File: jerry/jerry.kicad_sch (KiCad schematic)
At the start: 7 parts, among them U1 RASPBERRY_PI_4B_4GB

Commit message: Imported Parts
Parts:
- added J1, J2, J3: 0532610471, symbol jerry:0532610471
- added J4: XT60-M, symbol jerry:XT60-M
- added J7, J8: TSW-106-06-F-S-LL, symbol jerry:TSW-106-06-F-S-LL
- added U2: A4988_STEPPER_MOTOR_DRIVER_CARRIER, symbol jerry:A4988_STEPPER_MOTOR_DRIVER_CARRIER
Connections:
- new net: U2.15 (GND), U2.9 (GND)
- new net: J3.S1 (SHIELD), J3.S2 (SHIELD)
- new net: J1.S1 (SHIELD), J1.S2 (SHIELD)
- new net: J2.S1 (SHIELD), J2.S2 (SHIELD)
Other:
- moved on the sheet: D1, D2, D3, D4, D5, D6

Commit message: some updates
updated schematic, added components
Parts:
- added C1, C2, C3: .1uF, symbol Device:C_Polarized_US
- added C4: 1uF, symbol Device:C_Polarized_US
- added C5: 10uF, symbol Device:C_Polarized_US
- added D7: LED, Diode_SMD:D_0201_0603Metric_Pad0.64x0.40mm_HandSolder, symbol Device:LED
- added F1: Fuse, symbol Device:Fuse
- added R1, R7: 2k, symbol Device:R_US
- added R2, R4, R5, R6: 1k, symbol Device:R_US
- added R3: 330, symbol Device:R_US
- added S1: 500SSP1S2M2QEA, SW_500SSP1S2M2QEA, symbol jerry:500SSP1S2M2QEA
- added U3, U4: LM338T, jerry:TO254P1054X470X1955-3, symbol jerry:LM338T
- J1, J2, J3: footprint (none) -> jerry:MOLEX_0532610471
- J4: footprint (none) -> jerry:AMASS_XT60-M
- J7, J8: footprint (none) -> jerry:SAMTEC_TSW-106-06-F-S-LL
- U2: footprint (none) -> jerry:MODULE_A4988_STEPPER_MOTOR_DRIVER_CARRIER
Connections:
- net at D3.1 (K): now also R3.1
- net +5V: now reaches D3.2 (A)
- net +5V: now also J1.1, J2.1, J3.1, C1.1, C2.1, C3.1
- net at D6.1 (K): now also R6.1
- net LEDInd3: now reaches D6.2 (A)
- net TFMINIRX3: now reaches J3.2
- net TFMINITX3: now reaches J3.3
- net GND: now reaches J3.4
- net GND: now also J1.4, J1.S1 (SHIELD), J1.S2 (SHIELD), J2.4, J2.S1 (SHIELD), J2.S2 (SHIELD), J3.S1 (SHIELD), J3.S2 (SHIELD), J4.N (NEG), C1.2, C2.2, C3.2, C4.2, C5.2, R1.2, R2.2, R3.2, R4.2, R5.2, R6.2, R7.1
- net at J4.P (POS): now also F1.1
- net at D4.1 (K): now also R4.1
- net LEDInd1: now reaches D4.2 (A)
- net TFMINIRX1: now reaches J1.2
- net TFMINITX1: now reaches J1.3
- net at D1.1 (K): now also R1.1
- net +24V: now reaches D1.2 (A)
- net +24V: now also C4.1, C5.1, D7.2 (A), S1.2
- net at D2.1 (K): now also R2.1
- net +12V: now reaches D2.2 (A)
- net TFMINIRX2: now reaches J2.2
- net TFMINITX2: now reaches J2.3
- net at D5.1 (K): now also R5.1
- net LEDInd2: now reaches D5.2 (A)
- new net: D7.1 (K), R7.2
- new net: F1.2, S1.3
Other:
- note added: "Encoder"
- note added: "Motor Driver"
- note added: "Power Input"
- note added: "Raspberry Pi"
- note added: "TF Mini"
- note added: "Voltage Regulators"
- moved on the sheet: D1, D2, D3, D4, D5, D6, J1, J2, J3, J4, J7, J8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

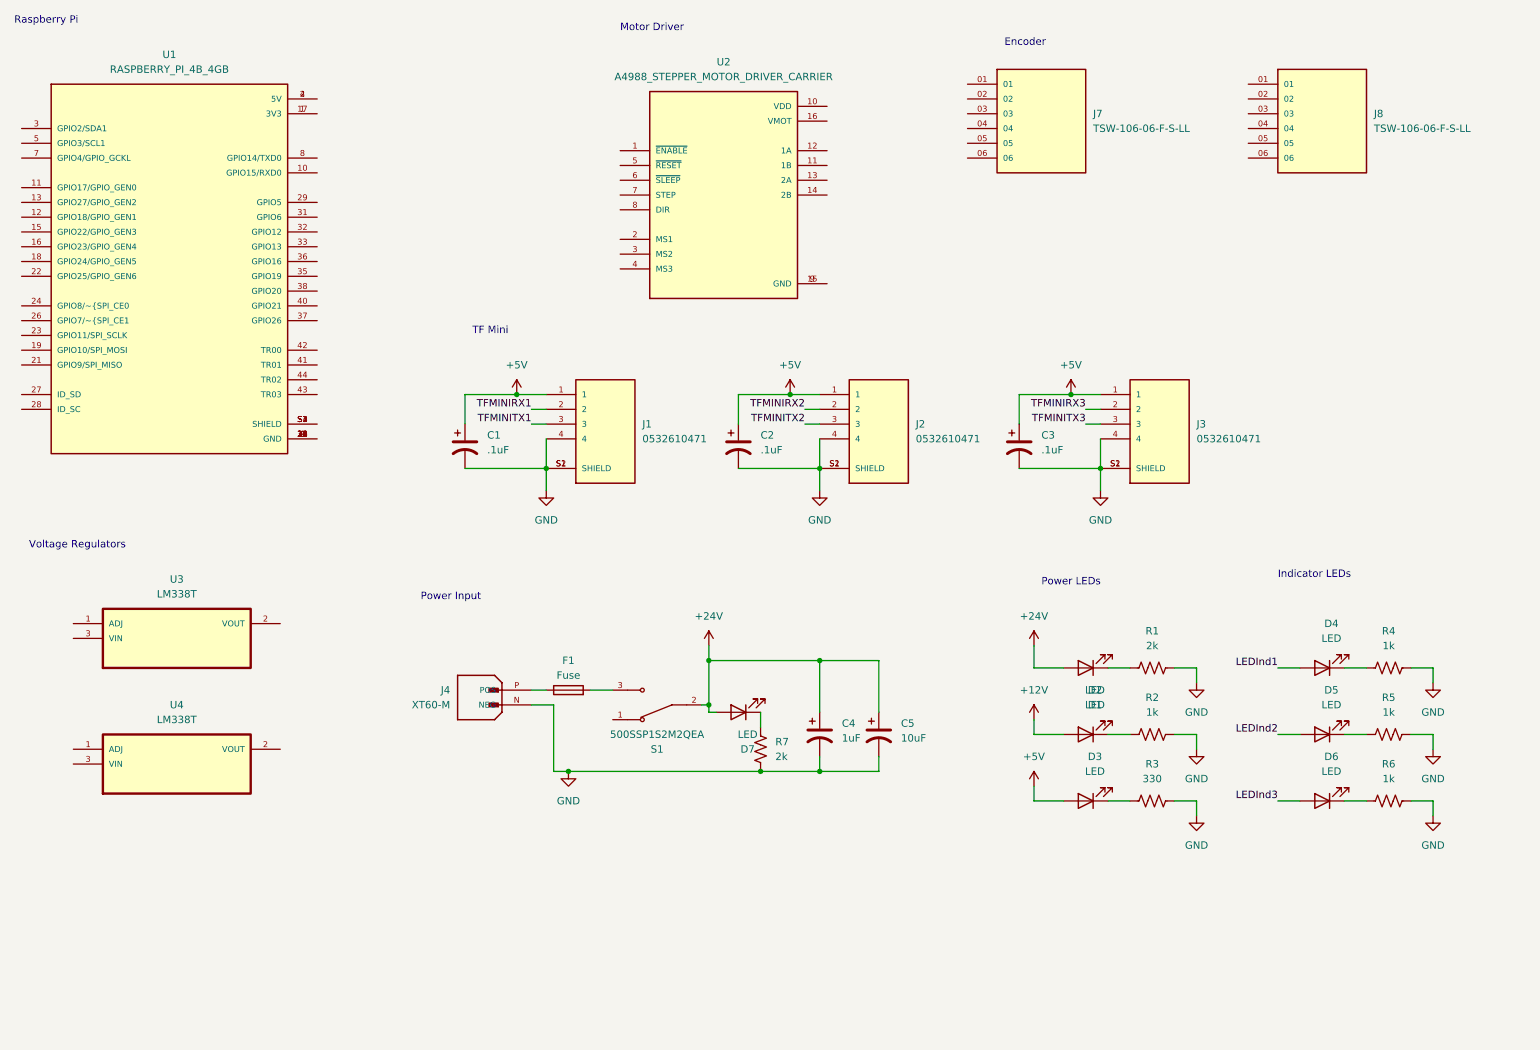
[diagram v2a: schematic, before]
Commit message: Voltage regulators. encoders
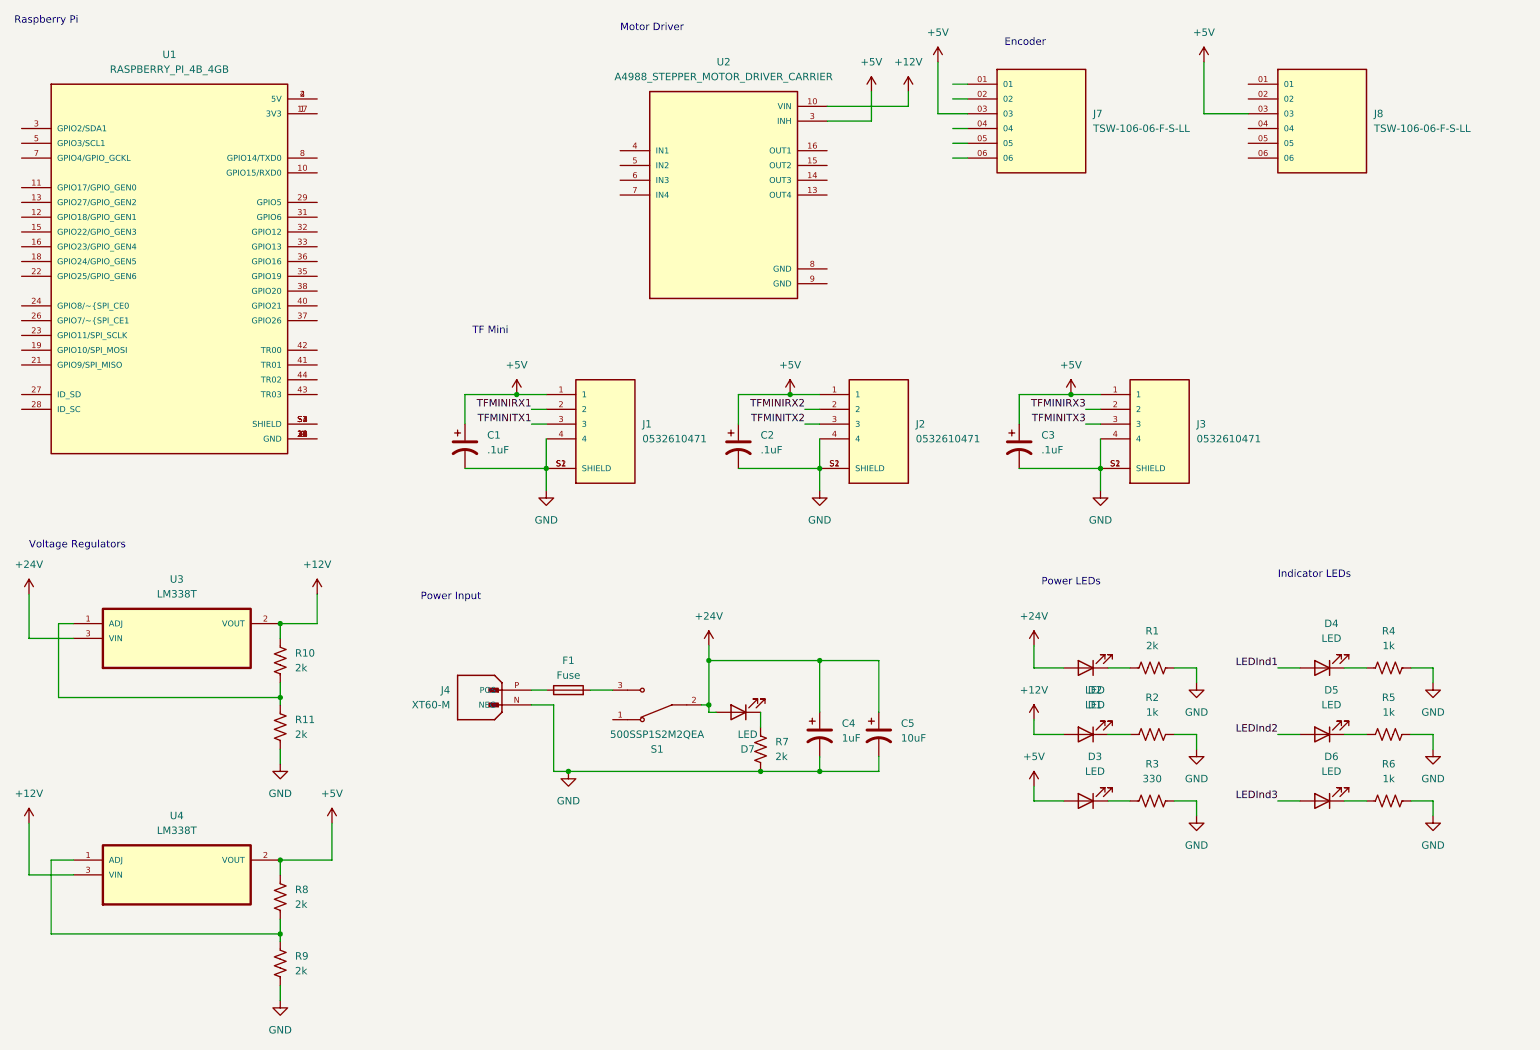
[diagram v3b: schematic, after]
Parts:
- added R10, R11, R8, R9: 2k, symbol Device:R_US
- S1: footprint SW_500SSP1S2M2QEA -> jerry:SW_500SSP1S2M2QEA
- U2: footprint jerry:MODULE_A4988_STEPPER_MOTOR_DRIVER_CARRIER -> (none)
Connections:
- net +12V: now also U2.10 (VIN), U3.2 (VOUT), U4.3 (VIN), R10.2
- net +24V: now also U3.3 (VIN)
- net +5V: now also J7.03, J8.03, U2.3 (INH), U4.2 (VOUT), R8.2
- net GND: now also R11.1, R9.1
- net at U2.15 (OUT2): no longer U2.9 (GND)
- net at U3.1 (ADJ): now also R10.1, R11.2
- net at U4.1 (ADJ): now also R8.1, R9.2
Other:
- moved on the sheet: U4
